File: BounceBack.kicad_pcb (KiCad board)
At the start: 2 copper layers, 33 parts, among them Q1 IRFS4229

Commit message: fix footprints and layout board
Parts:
- moved BT16 487.5 mm to (502.8, -82.4)
- moved BT24 487.5 mm to (502.8, -60.3)
- moved BT32 487.5 mm to (502.8, -38.1)
- moved BT8 487.5 mm to (502.8, -104.5)
- moved BT15 369.6 mm to (442.5, -82.6)
- moved BT23 369.6 mm to (442.5, -60.5)
- moved BT31 369.6 mm to (442.5, -38.4)
- moved BT7 369.6 mm to (442.5, -104.8)
- moved BT13 354.0 mm to (314.5, -84.1)
- moved BT5 354.0 mm to (314.5, -106.2)
- moved BT21 354.0 mm to (314.5, -62.0)
- moved BT29 354.0 mm to (314.5, -39.9)
- moved BT14 343.8 mm to (389.0, -81.6)
- moved BT6 343.8 mm to (389.0, -103.8)
- moved BT22 343.8 mm to (389.0, -59.5)
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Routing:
- net /Battery Pack/4.2v: track 0.00 -> 179.2 mm
- net /Battery Pack/8.4v: track 0.00 -> 89.5 mm
- net /Battery Pack/0v: track 0.00 -> 89.5 mm

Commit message: finish battery terminal placement
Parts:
- removed Q1: IRFS4229, Package_TO_SOT_SMD:TO-263-2
- moved BT24 384.2 mm to (122.0, -9.00), turned to 180 degrees
- moved BT32 384.2 mm to (122.0, 13.0), turned to 180 degrees
- moved BT8 351.0 mm to (172.0, 13.0)
- moved BT23 341.7 mm to (122.0, 58.0), turned to 180 degrees
- moved BT16 338.8 mm to (172.0, -9.00)
- moved BT31 329.0 mm to (122.0, 36.0), turned to 180 degrees
- moved BT7 315.7 mm to (172.0, 58.0)
- moved BT4 313.8 mm to (42.0, 126.0), turned to 180 degrees
- moved BT12 313.7 mm to (42.0, 148.0), turned to 180 degrees
- moved BT22 312.6 mm to (122.0, 103.0), turned to 180 degrees
- moved BT15 295.4 mm to (172.0, 36.0)
- moved BT30 292.1 mm to (122.0, 81.0), turned to 180 degrees
- moved BT5 291.5 mm to (172.0, 148.0)
- moved BT6 285.0 mm to (172.0, 81.0)
- moved BT14 284.9 mm to (172.0, 103.0)
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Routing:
- net /Battery Pack/29.4: track 0.00 -> 367.4 mm
- net /Battery Pack/25.2: track 0.00 -> 322.0 mm
- net /Battery Pack/12.6v: track 0.00 -> 277.0 mm
- net /Battery Pack/21v: track 0.00 -> 276.6 mm
- net /Battery Pack/16.8v: track 0.00 -> 270.4 mm
- net /Battery Pack/33.6: track 0.00 -> 240.1 mm
- net /Battery Pack/8.4v: track 89.5 -> 321.9 mm
- net /Battery Pack/4.2v: track 179.2 -> 366.9 mm
- net /Battery Pack/0v: track 89.5 -> 240.9 mm
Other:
- board outline added: 221 x 202 mm

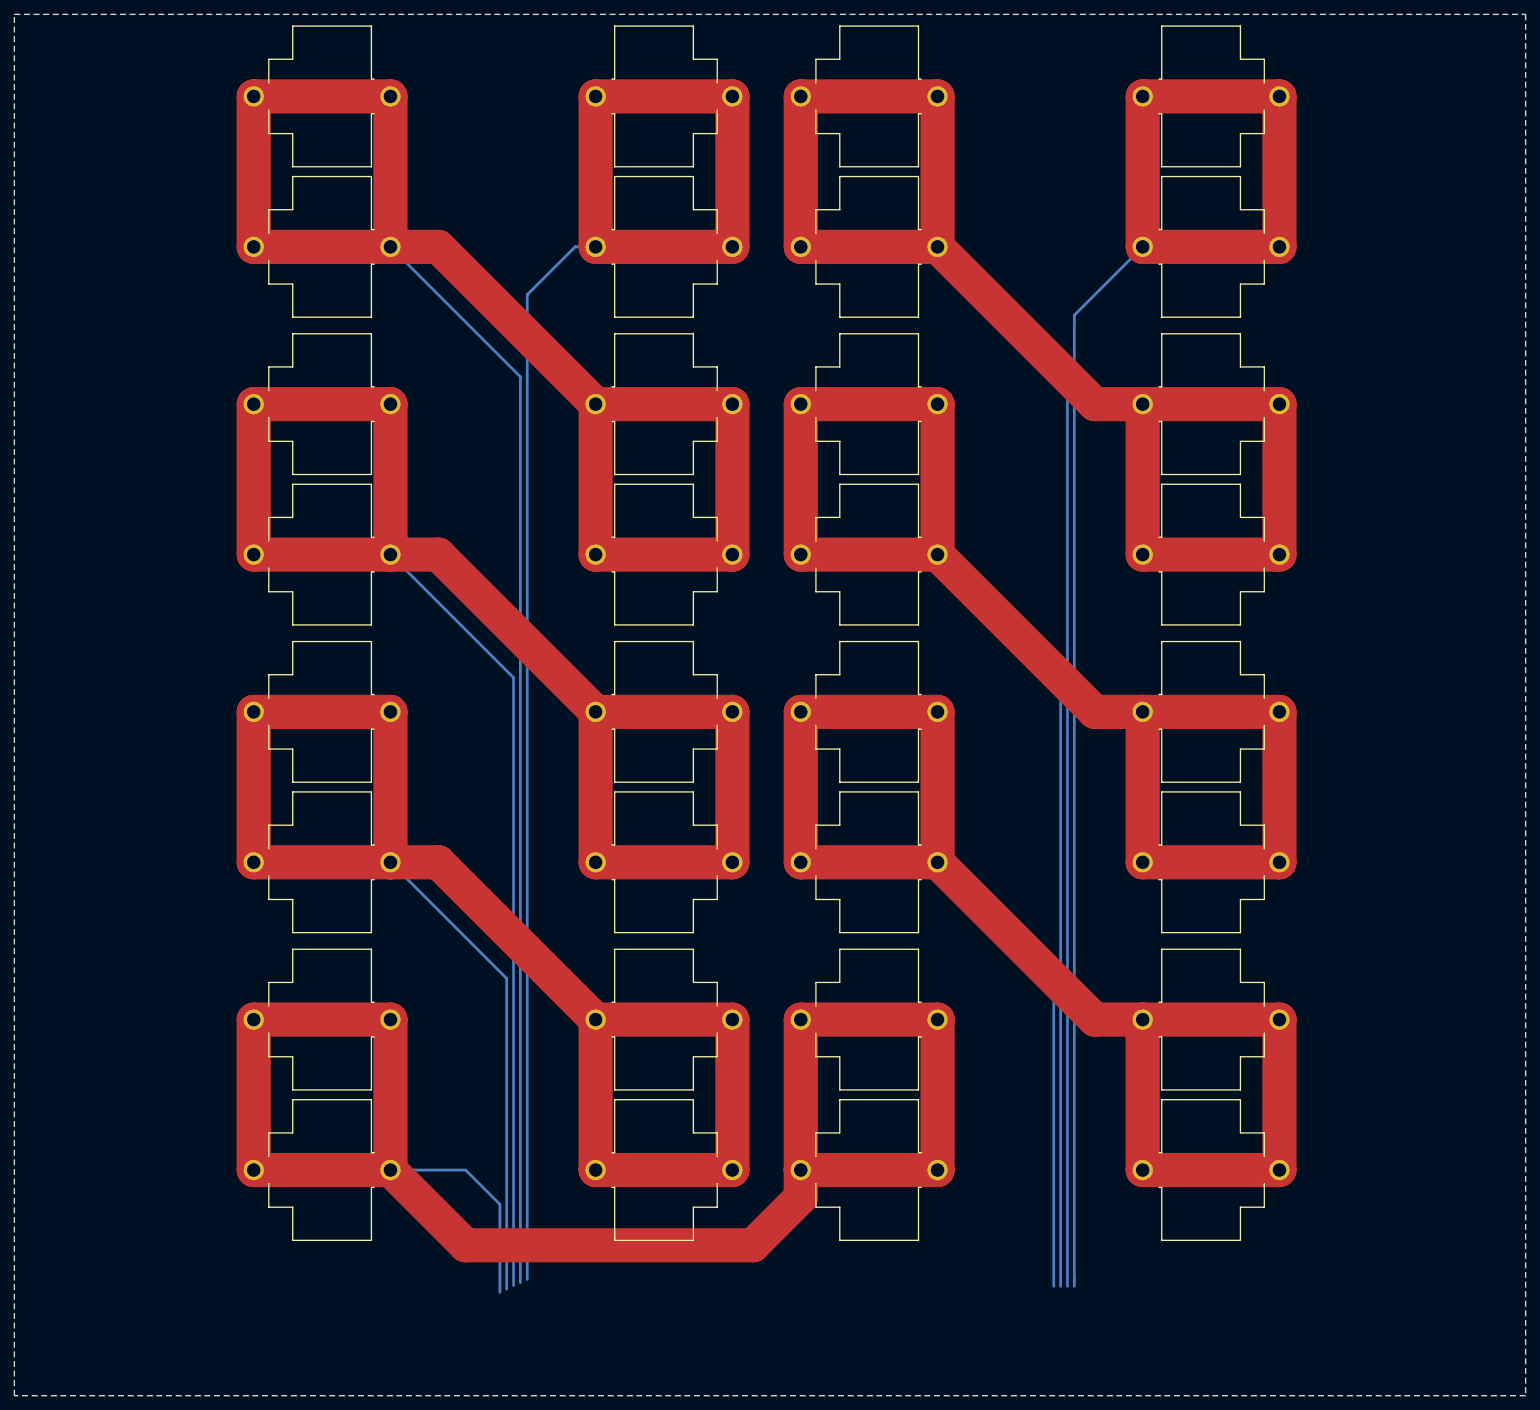
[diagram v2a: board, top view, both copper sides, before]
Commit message: adds connectors and bom
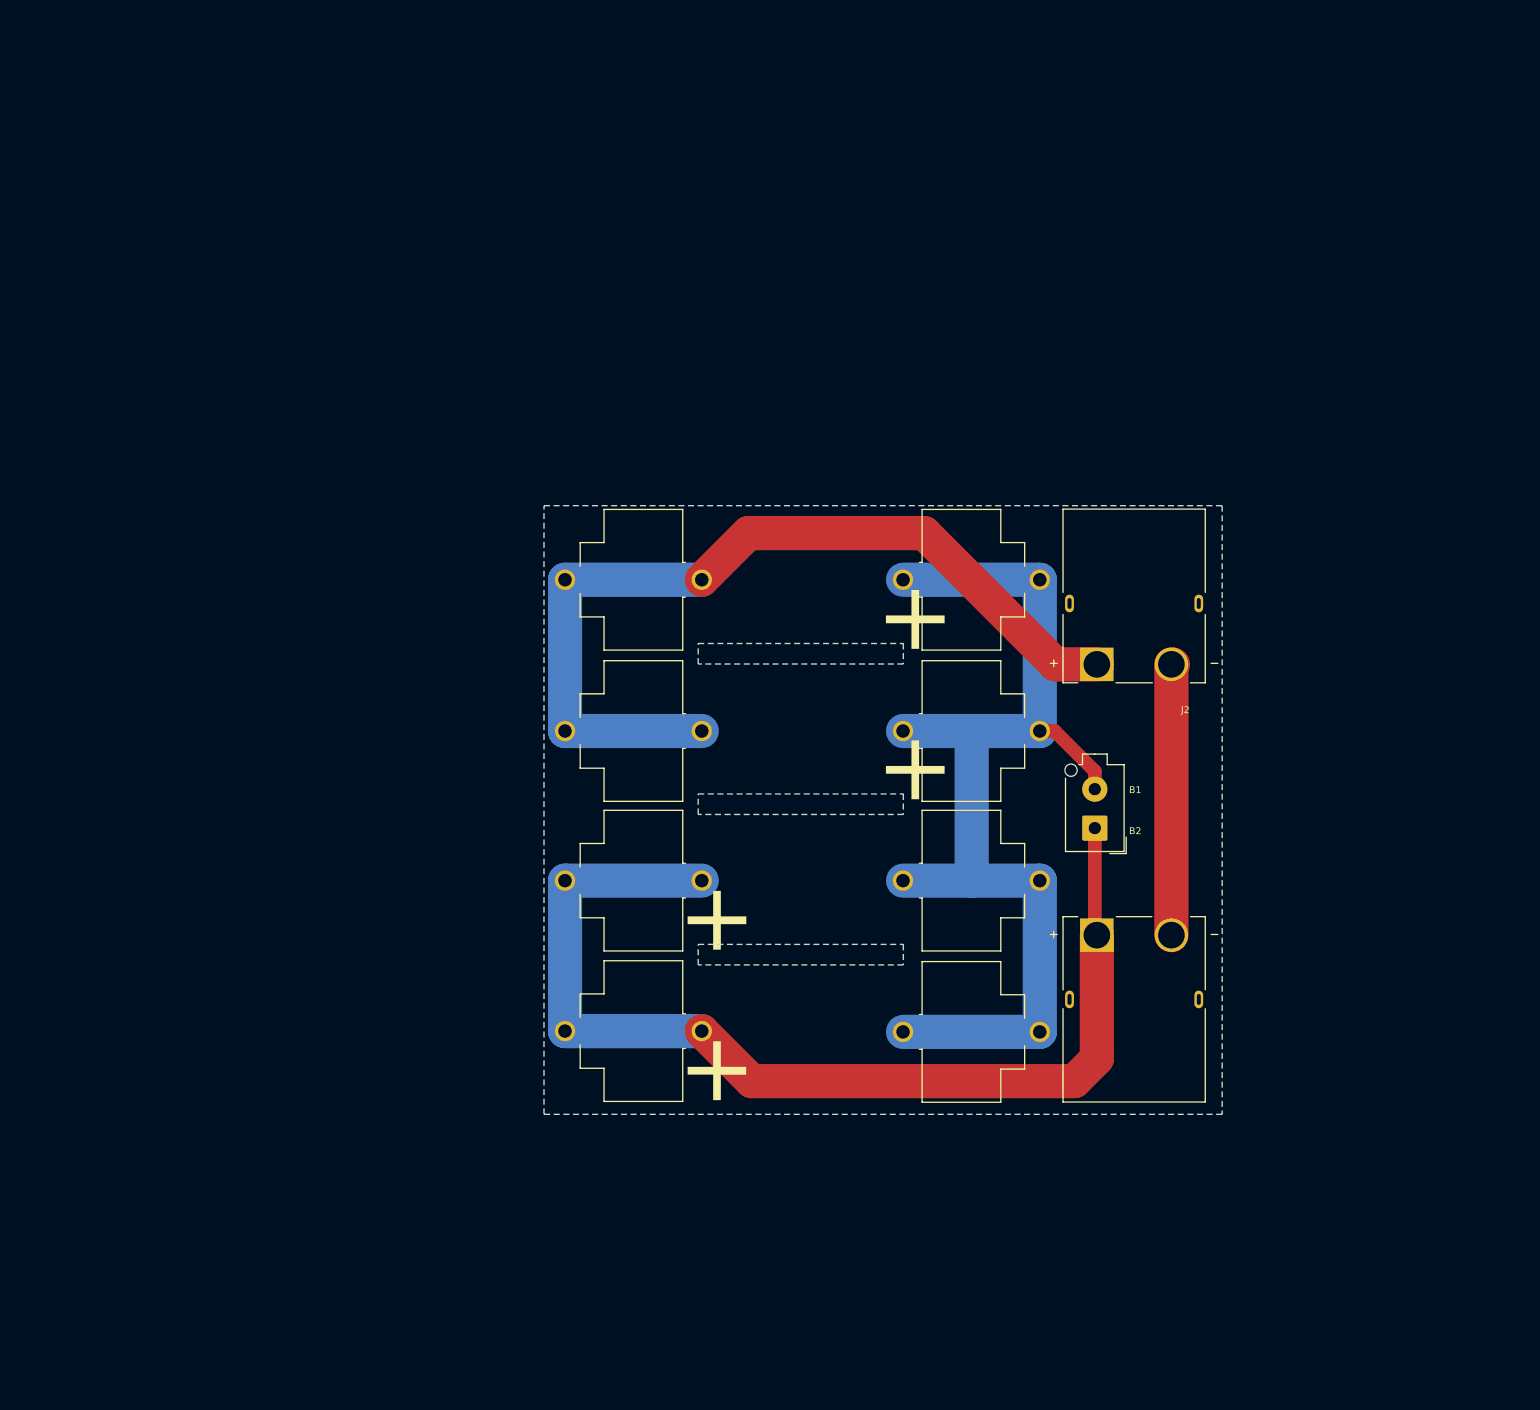
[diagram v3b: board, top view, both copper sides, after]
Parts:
- removed BT1, BT10, BT11, BT12, BT13, BT14, BT15, BT16, BT17, BT18, BT19, BT2, BT20, BT21, BT22, BT23, BT24, BT25, BT26, BT27, BT28, BT29, BT3, BT30, BT31, BT32, BT4, BT5, BT6, BT7, BT8, BT9: 246, 246:BAT_246
- added BT33: 246, 246:BAT_246, F.Cu at (137.0, 61.7)
- added BT34: 246, 246:BAT_246, F.Cu at (137.0, 83.8)
- added BT35: 246, 246:BAT_246, F.Cu at (87.5, 83.8)
- added BT36: 246, 246:BAT_246, F.Cu at (87.5, 61.7)
- added BT37: 246, 246:BAT_246, F.Cu at (87.5, 105.7)
- added BT38: 246, 246:BAT_246, F.Cu at (87.5, 127.7)
- added BT39: 246, 246:BAT_246, F.Cu at (137.0, 127.8)
- added BT40: 246, 246:BAT_246, F.Cu at (137.0, 105.7)
- added J1: XT90PW-M, XT90PW-M:AMASS_XT90PW-M, F.Cu at (160.8, 123.0)
- added J2: XT90PW-F, XT90PW-F:AMASS_XT90PW-F, F.Cu at (160.8, 65.2)
- added J3: Conn_01x02_Socket, Connector_Molex:Molex_Mega-Fit_76829-0102_2x01_P5.70mm_Vertical, F.Cu at (155.0, 98.0)
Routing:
- net /Battery Pack/29.4: track 367.4 -> 0.00 mm
- net /Battery Pack/4.2v: track 366.9 -> 0.00 mm
- net /Battery Pack/25.2: track 322.0 -> 0.00 mm
- net /Battery Pack/8.4v: track 321.9 -> 0.00 mm
- net /Battery Pack/12.6v: track 277.0 -> 0.00 mm
- net /Battery Pack/21v: track 276.6 -> 0.00 mm
- net /Battery Pack/16.8v: track 270.4 -> 0.00 mm
- net /Battery Pack/0v: track 240.9 -> 0.00 mm
- net /Battery Pack/33.6: track 240.1 -> 0.00 mm
- net /Battery1/BAT+: track 0.00 -> 159.2 mm
- net /Next_Cell: track 0.00 -> 158.0 mm
- net /Prev_Cell: track 0.00 -> 130.7 mm
- net Net-(J1-NEG): track 0.00 -> 39.9 mm
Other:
- board size 221 x 202 mm -> 99.2 x 89 mm
- board text added: "+"
- board text added: "B1"
- board text added: "B2"
